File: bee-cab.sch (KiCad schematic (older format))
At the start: 26 parts, among them J1 Conn_01x02_Male, J10 Conn_01x01, J11 Conn_02x01, J12 Conn_02x01, J13 Conn_01x02, J14 Conn_01x02, J15 Conn_01x02, J16 Conn_01x02, J17 Conn_01x03, J18 Conn_01x02, J19 Conn_01x02, J2 Conn_01x02_Male, J3 Conn_01x02_Male, J4 Conn_01x02_Male, J5 Conn_01x03, J6 Conn_02x03_Odd_Even, J7 Conn_02x01, J8 Conn_01x02, J9 Conn_01x02

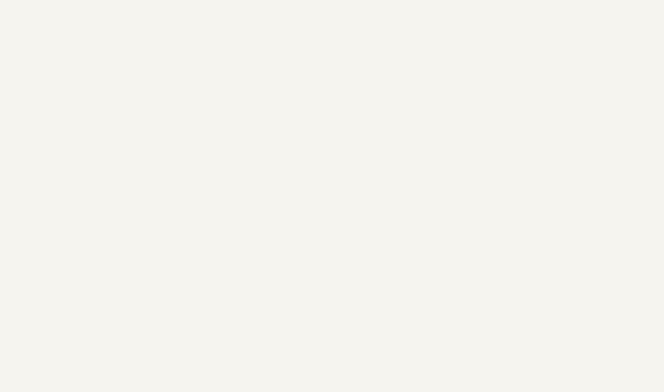
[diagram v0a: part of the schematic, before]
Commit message: Add sch symbols for labels, update PCB accordingly.
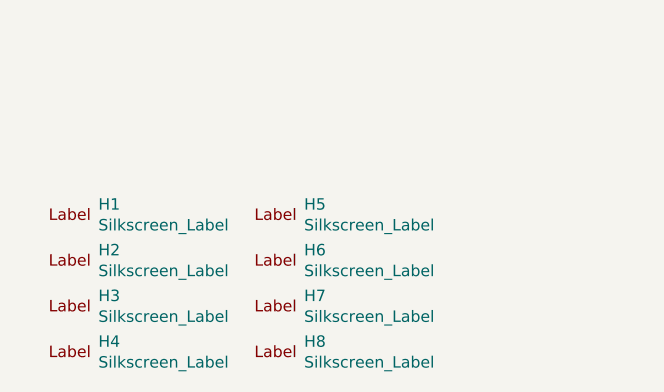
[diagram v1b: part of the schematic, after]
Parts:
- added H1, H2: Silkscreen_Label, Symbol-emt:Text_U_B+_Silkscreen, symbol Mechanical-emt:Silkscreen_Label
- added H3, H4: Silkscreen_Label, Symbol-emt:Text_U_B-_Silkscreen, symbol Mechanical-emt:Silkscreen_Label
- added H5, H6: Silkscreen_Label, Symbol-emt:Text_U_B2_Silkscreen, symbol Mechanical-emt:Silkscreen_Label
- added H7, H8: Silkscreen_Label, Symbol-emt:Symbol_GND_Silkscreen, symbol Mechanical-emt:Silkscreen_Label
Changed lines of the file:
@@
 Wire Wire Line
 	2600 2900 2600 3050
+$Comp
+L Mechanical-emt:Silkscreen_Label H4
+U 1 1 5CC7DACB
+P 800 7550
+F 0 "H4" H 925 7595 50  0000 L CNN
+F 1 "Silkscreen_Label" H 925 7504 50  0000 L CNN
+F 2 "Symbol-emt:Text_U_B-_Silkscreen" H 800 7550 50  0001 C CNN
+F 3 "~" H 800 7550 50  0001 C CNN
+	1    800  7550
+	1    0    0    -1
+$EndComp
+$Comp
+L Mechanical-emt:Silkscreen_Label H3
+U 1 1 5CC7E4B0
+P 800 7350
+F 0 "H3" H 925 7395 50  0000 L CNN
+F 1 "Silkscreen_Label" H 925 7304 50  0000 L CNN
+F 2 "Symbol-emt:Text_U_B-_Silkscreen" H 800 7350 50  0001 C CNN
+F 3 "~" H 800 7350 50  0001 C CNN
+	1    800  7350
+	1    0    0    -1
+$EndComp
+$Comp
+L Mechanical-emt:Silkscreen_Label H2
+U 1 1 5CC7E7BF
+P 800 7150
+F 0 "H2" H 925 7195 50  0000 L CNN
+F 1 "Silkscreen_Label" H 925 7104 50  0000 L CNN
+F 2 "Symbol-emt:Text_U_B+_Silkscreen" H 800 7150 50  0001 C CNN
+F 3 "~" H 800 7150 50  0001 C CNN
+	1    800  7150
+	1    0    0    -1
+$EndComp
+$Comp
+L Mechanical-emt:Silkscreen_Label H1
+U 1 1 5CC7EB64
+P 800 6950
+F 0 "H1" H 925 6995 50  0000 L CNN
+F 1 "Silkscreen_Label" H 925 6904 50  0000 L CNN
+F 2 "Symbol-emt:Text_U_B+_Silkscreen" H 800 6950 50  0001 C CNN
+F 3 "~" H 800 6950 50  0001 C CNN
+	1    800  6950
+	1    0    0    -1
+$EndComp
+$Comp
+L Mechanical-emt:Silkscreen_Label H5
+U 1 1 5CC7EED7
+P 1700 6950
+F 0 "H5" H 1825 6995 50  0000 L CNN
+F 1 "Silkscreen_Label" H 1825 6904 50  0000 L CNN
+F 2 "Symbol-emt:Text_U_B2_Silkscreen" H 1700 6950 50  0001 C CNN
+F 3 "~" H 1700 6950 50  0001 C CNN
+	1    1700 6950
+	1    0    0    -1
+$EndComp
+$Comp
+L Mechanical-emt:Silkscreen_Label H6
+U 1 1 5CC7F429
+P 1700 7150
+F 0 "H6" H 1825 7195 50  0000 L CNN
+F 1 "Silkscreen_Label" H 1825 7104 50  0000 L CNN
+F 2 "Symbol-emt:Text_U_B2_Silkscreen" H 1700 7150 50  0001 C CNN
+F 3 "~" H 1700 7150 50  0001 C CNN
+	1    1700 7150
+	1    0    0    -1
+$EndComp
+$Comp
+L Mechanical-emt:Silkscreen_Label H7
+U 1 1 5CC7F75B
+P 1700 7350
+F 0 "H7" H 1825 7395 50  0000 L CNN
+F 1 "Silkscreen_Label" H 1825 7304 50  0000 L CNN
+F 2 "Symbol-emt:Symbol_GND_Silkscreen" H 1700 7350 50  0001 C CNN
+F 3 "~" H 1700 7350 50  0001 C CNN
+	1    1700 7350
+	1    0    0    -1
+$EndComp
+$Comp
+L Mechanical-emt:Silkscreen_Label H8
+U 1 1 5CC7FA9C
+P 1700 7550
+F 0 "H8" H 1825 7595 50  0000 L CNN
+F 1 "Silkscreen_Label" H 1825 7504 50  0000 L CNN
+F 2 "Symbol-emt:Symbol_GND_Silkscreen" H 1700 7550 50  0001 C CNN
+F 3 "~" H 1700 7550 50  0001 C CNN
+	1    1700 7550
+	1    0    0    -1
+$EndComp
 $EndSCHEMATC

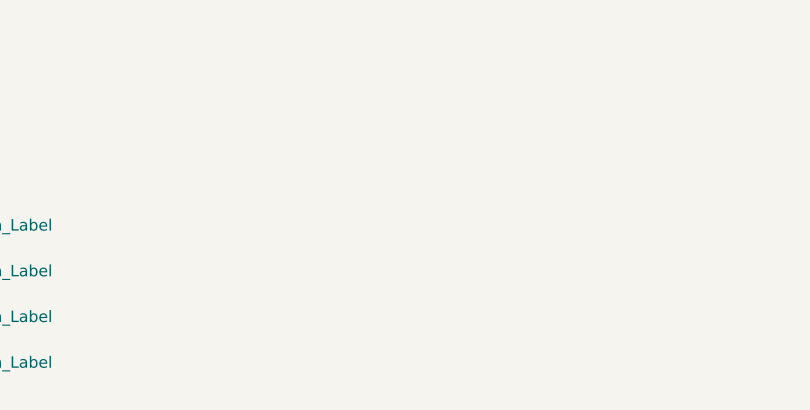
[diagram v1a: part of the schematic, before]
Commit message: Replace vias by mounting holes.
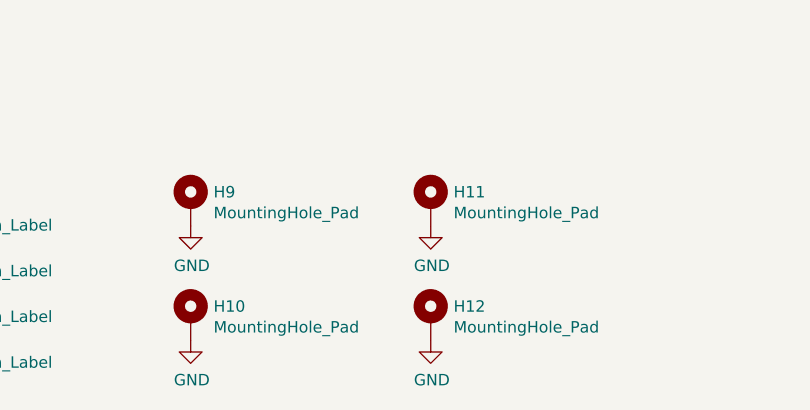
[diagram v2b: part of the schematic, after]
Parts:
- added H10, H11, H12, H9: MountingHole_Pad, MountingHole:MountingHole_3.2mm_M3_ISO7380_Pad, symbol Mechanical:MountingHole_Pad
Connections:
- net GND: now also H10.1, H11.1, H12.1, H9.1
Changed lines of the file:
@@
+	1    0    0    -1
+$EndComp
+$Comp
+L Mechanical:MountingHole_Pad H10
+U 1 1 5CC731BF
+P 3000 7400
+F 0 "H10" H 3100 7449 50  0000 L CNN
+F 1 "MountingHole_Pad" H 3100 7358 50  0000 L CNN
+F 2 "MountingHole:MountingHole_3.2mm_M3_ISO7380_Pad" H 3000 7400 50  0001 C CNN
+F 3 "~" H 3000 7400 50  0001 C CNN
+	1    3000 7400
+	1    0    0    -1
+$EndComp
+$Comp
+L power:GND #PWR0101
+U 1 1 5CC74B62
+P 3000 7500
+F 0 "#PWR0101" H 3000 7250 50  0001 C CNN
+F 1 "GND" H 3005 7327 50  0000 C CNN
+F 2 "" H 3000 7500 50  0001 C CNN
+F 3 "" H 3000 7500 50  0001 C CNN
+	1    3000 7500
+	1    0    0    -1
+$EndComp
+$Comp
+L Mechanical:MountingHole_Pad H9
+U 1 1 5CC7CF5D
+P 3000 6900
+F 0 "H9" H 3100 6949 50  0000 L CNN
+F 1 "MountingHole_Pad" H 3100 6858 50  0000 L CNN
+F 2 "MountingHole:MountingHole_3.2mm_M3_ISO7380_Pad" H 3000 6900 50  0001 C CNN
+F 3 "~" H 3000 6900 50  0001 C CNN
+	1    3000 6900
+	1    0    0    -1
+$EndComp
+$Comp
+L power:GND #PWR0102
+U 1 1 5CC7CF67
+P 3000 7000
+F 0 "#PWR0102" H 3000 6750 50  0001 C CNN
+F 1 "GND" H 3005 6827 50  0000 C CNN
+F 2 "" H 3000 7000 50  0001 C CNN
+F 3 "" H 3000 7000 50  0001 C CNN
+	1    3000 7000
+	1    0    0    -1
+$EndComp
+$Comp
+L Mechanical:MountingHole_Pad H12
+U 1 1 5CC82F8F
+P 4050 7400
+F 0 "H12" H 4150 7449 50  0000 L CNN
+F 1 "MountingHole_Pad" H 4150 7358 50  0000 L CNN
+F 2 "MountingHole:MountingHole_3.2mm_M3_ISO7380_Pad" H 4050 7400 50  0001 C CNN
+F 3 "~" H 4050 7400 50  0001 C CNN
+	1    4050 7400
+	1    0    0    -1
+$EndComp
+$Comp
+L power:GND #PWR0103
+U 1 1 5CC82F99
+P 4050 7500
+F 0 "#PWR0103" H 4050 7250 50  0001 C CNN
+F 1 "GND" H 4055 7327 50  0000 C CNN
+F 2 "" H 4050 7500 50  0001 C CNN
+F 3 "" H 4050 7500 50  0001 C CNN
+	1    4050 7500
+	1    0    0    -1
+$EndComp
+$Comp
+L Mechanical:MountingHole_Pad H11
+U 1 1 5CC82FA3
+P 4050 6900
+F 0 "H11" H 4150 6949 50  0000 L CNN
+F 1 "MountingHole_Pad" H 4150 6858 50  0000 L CNN
+F 2 "MountingHole:MountingHole_3.2mm_M3_ISO7380_Pad" H 4050 6900 50  0001 C CNN
+F 3 "~" H 4050 6900 50  0001 C CNN
+	1    4050 6900
+	1    0    0    -1
+$EndComp
+$Comp
+L power:GND #PWR0104
+U 1 1 5CC82FAD
+P 4050 7000
+F 0 "#PWR0104" H 4050 6750 50  0001 C CNN
+F 1 "GND" H 4055 6827 50  0000 C CNN
+F 2 "" H 4050 7000 50  0001 C CNN
+F 3 "" H 4050 7000 50  0001 C CNN
+	1    4050 7000
 	1    0    0    -1
 $EndComp

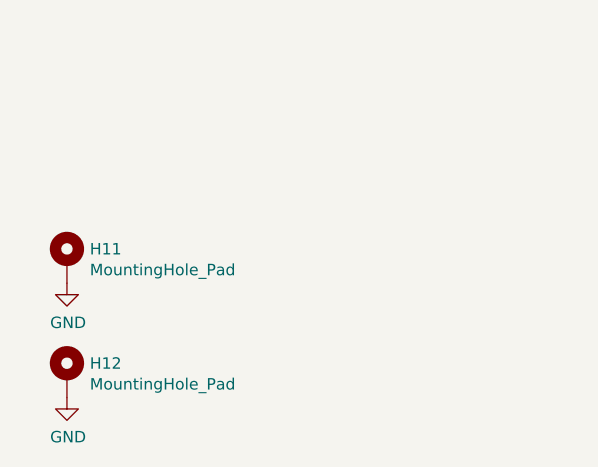
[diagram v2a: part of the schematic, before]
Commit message: Add text and logos.
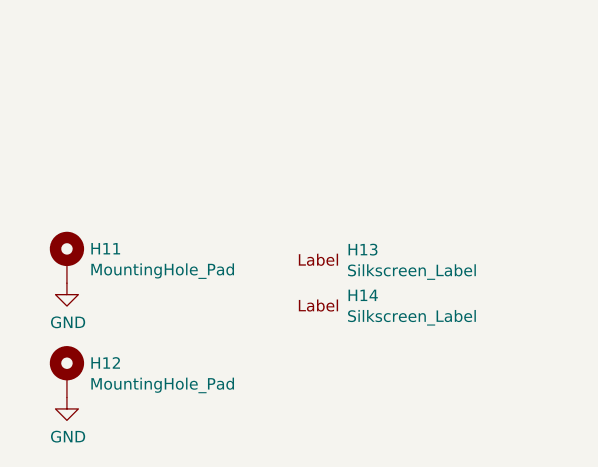
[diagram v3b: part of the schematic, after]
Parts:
- added H13: Silkscreen_Label, Symbol-emt:EMT-Logo_5.1x2.5mm_Silkscreen, symbol Mechanical-emt:Silkscreen_Label
- added H14: Silkscreen_Label, Symbol-emt:BEE-Logo_Silkscreen_small, symbol Mechanical-emt:Silkscreen_Label
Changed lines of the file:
@@
 EESchema Schematic File Version 4
 LIBS:bee-cab-cache
-EELAYER 29 0
+EELAYER 26 0
 EELAYER END
 $Descr A4 11693 8268
@@
 	1    0    0    -1
 $EndComp
+$Comp
+L Mechanical-emt:Silkscreen_Label H13
+U 1 1 5CCCFACF
+P 5150 6900
+F 0 "H13" H 5275 6945 50  0000 L CNN
+F 1 "Silkscreen_Label" H 5275 6854 50  0000 L CNN
+F 2 "Symbol-emt:EMT-Logo_5.1x2.5mm_Silkscreen" H 5150 6900 50  0001 C CNN
+F 3 "~" H 5150 6900 50  0001 C CNN
+	1    5150 6900
+	1    0    0    -1
+$EndComp
+$Comp
+L Mechanical-emt:Silkscreen_Label H14
+U 1 1 5CCCFB83
+P 5150 7100
+F 0 "H14" H 5275 7145 50  0000 L CNN
+F 1 "Silkscreen_Label" H 5275 7054 50  0000 L CNN
+F 2 "Symbol-emt:BEE-Logo_Silkscreen_small" H 5150 7100 50  0001 C CNN
+F 3 "~" H 5150 7100 50  0001 C CNN
+	1    5150 7100
+	1    0    0    -1
+$EndComp

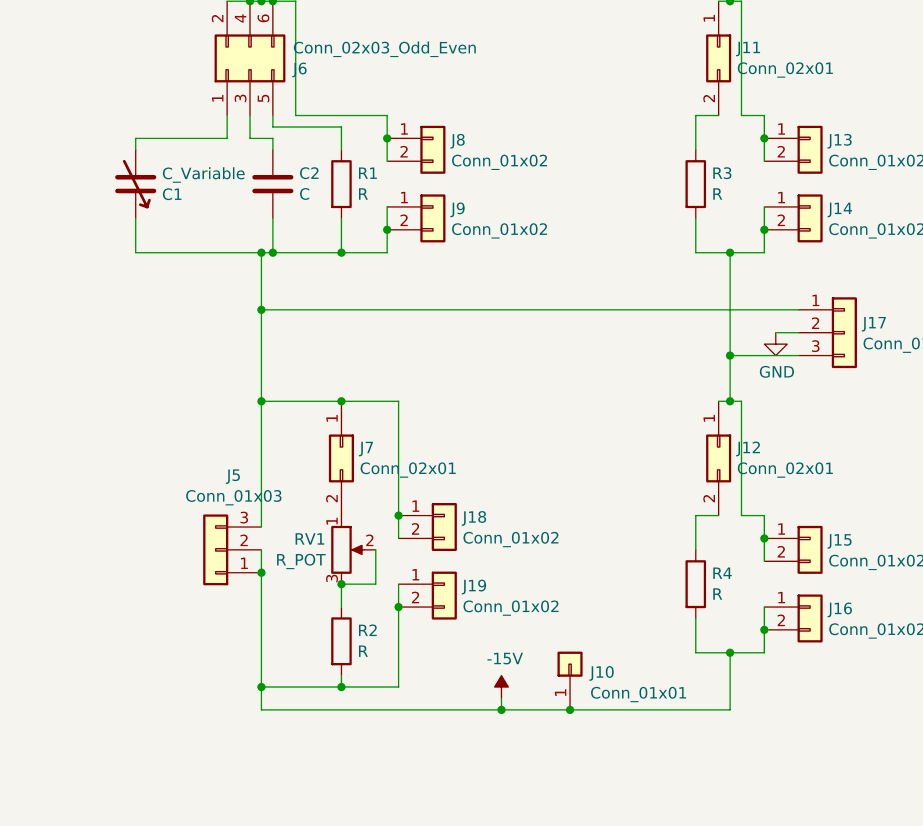
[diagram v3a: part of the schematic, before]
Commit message: Add part numbers.
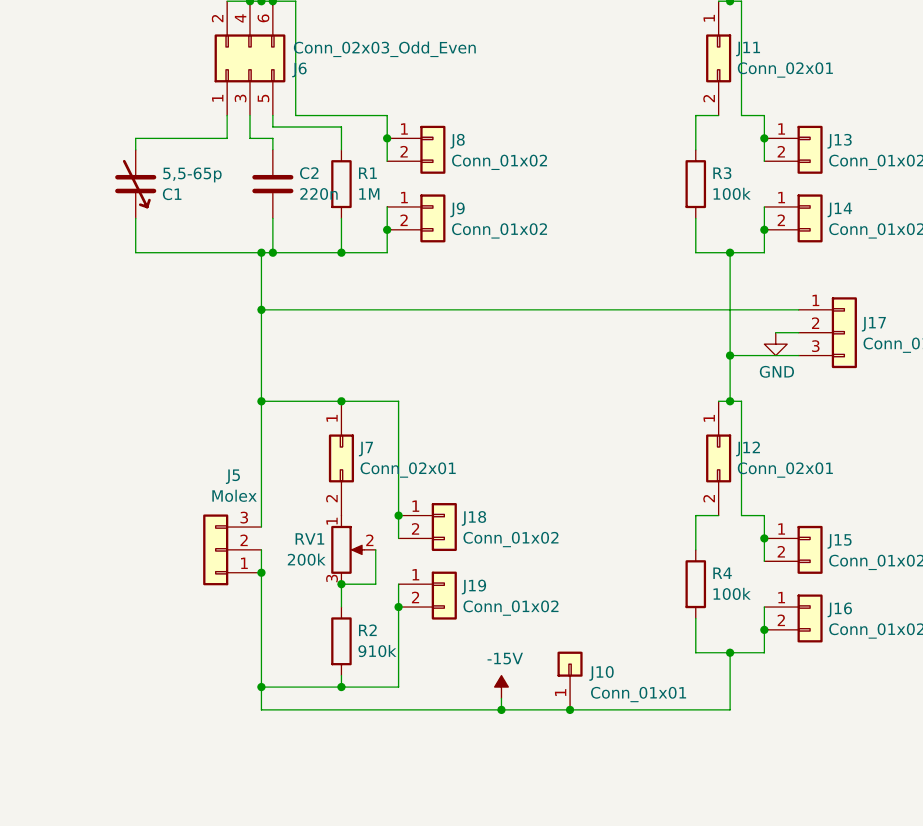
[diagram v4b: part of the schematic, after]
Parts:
- C1: value C_Variable -> 5,5-65p; Reichelt Part No (none) -> TRIMMER 31659
- C2: value C -> 220n; Reichelt Part No (none) -> X7R 0805 CF 220N
- J1, J11, J12, J2, J3, J4, J7: Reichelt Part No (none) -> RND 205-00623
- J10: Reichelt Part No (none) -> RND 205-00622
- J13, J14, J15, J16, J18, J19, J8, J9: Reichelt Part No (none) -> MPE 006-1-002
- J17: Reichelt Part No (none) -> RND 205-00624
- J5: value Conn_01x03 -> Molex; Manufacturer (none) -> Molex; Manufacturer Part No (none) -> 52807-0310; Mouser Part No (none) -> 538-52807-0310
- J6: Reichelt Part No (none) -> RND 205-00634
- R1: value R -> 1M; Reichelt Part No (none) -> RND 0805 1 1,0M
- R2: value R -> 910k; Reichelt Part No (none) -> RND 0805 1 910K
- R3, R4: value R -> 100k; Reichelt Part No (none) -> RND 0805 1 100K
- RV1: value R_POT -> 200k; Reichelt Part No (none) -> 64W-200K
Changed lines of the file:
@@
 F 2 "Connector_PinHeader_2.54mm:PinHeader_1x02_P2.54mm_Vertical" H 850 1300 50  0001 C CNN
 F 3 "~" H 850 1300 50  0001 C CNN
+F 4 "RND 205-00623" H 850 1300 50  0001 C CNN "Reichelt Part No"
 	1    850  1300
 	1    0    0    -1
@@
 F 2 "Connector_PinHeader_2.54mm:PinHeader_1x02_P2.54mm_Vertical" H 850 950 50  0001 C CNN
 F 3 "~" H 850 950 50  0001 C CNN
+F 4 "RND 205-00623" H 850 950 50  0001 C CNN "Reichelt Part No"
 	1    850  950
 	1    0    0    -1
@@
 F 2 "Connector_PinHeader_2.54mm:PinHeader_1x02_P2.54mm_Vertical" H 850 2150 50  0001 C CNN
 F 3 "~" H 850 2150 50  0001 C CNN
+F 4 "RND 205-00623" H 850 2150 50  0001 C CNN "Reichelt Part No"
 	1    850  2150
 	1    0    0    -1
@@
 F 2 "Connector_PinHeader_2.54mm:PinHeader_1x02_P2.54mm_Vertical" H 850 1800 50  0001 C CNN
 F 3 "~" H 850 1800 50  0001 C CNN
+F 4 "RND 205-00623" H 850 1800 50  0001 C CNN "Reichelt Part No"
 	1    850  1800
 	1    0    0    -1
@@
 P 2600 2750
 F 0 "C1" H 2715 2796 50  0000 L CNN
-F 1 "C_Variable" H 2715 2705 50  0000 L CNN
+F 1 "5,5-65p" H 2715 2705 50  0000 L CNN
 F 2 "Capacitor_THT-emt:C_Trimmer_Vishay_D10mm_Vertical_HolePattern5mmx10mm" H 2600 2750 50  0001 C CNN
 F 3 "~" H 2600 2750 50  0001 C CNN
+F 4 "TRIMMER 31659" H 2600 2750 50  0001 C CNN "Reichelt Part No"
 	1    2600 2750
 	1    0    0    1
@@
 P 2950 4350
 F 0 "J5" H 2870 4025 50  0000 C CNN
-F 1 "Conn_01x03" H 2870 4116 50  0000 C CNN
+F 1 "Molex" H 2870 4116 50  0000 C CNN
 F 2 "Connector_Molex-emt:Molex_Easy-On_528070310_1x03_P1.0mm_Horizontal" H 2950 4350 50  0001 C CNN
 F 3 "~" H 2950 4350 50  0001 C CNN
+F 4 "538-52807-0310" H 2950 4350 50  0001 C CNN "Mouser Part No"
+F 5 "Molex" H 2950 4350 50  0001 C CNN "Manufacturer"
+F 6 "52807-0310" H 2950 4350 50  0001 C CNN "Manufacturer Part No"
 	1    2950 4350
 	-1   0    0    1
@@
 P 3200 2750
 F 0 "C2" H 3315 2796 50  0000 L CNN
-F 1 "C" H 3315 2705 50  0000 L CNN
+F 1 "220n" H 3315 2705 50  0000 L CNN
 F 2 "Capacitor_SMD:C_0805_2012Metric_Pad1.15x1.40mm_HandSolder" H 3238 2600 50  0001 C CNN
 F 3 "~" H 3200 2750 50  0001 C CNN
+F 4 "X7R 0805 CF 220N" H 3200 2750 50  0001 C CNN "Reichelt Part No"
 	1    3200 2750
 	1    0    0    -1
@@
 F 2 "Connector_PinSocket_2.54mm:PinSocket_2x01_P2.54mm_Vertical" H 3900 2550 50  0001 C CNN
 F 3 "~" H 3900 2550 50  0001 C CNN
+F 4 "MPE 006-1-002" H 3900 2550 50  0001 C CNN "Reichelt Part No"
 	1    3900 2550
 	1    0    0    -1
@@
 F 2 "Connector_PinSocket_2.54mm:PinSocket_2x01_P2.54mm_Vertical" H 3900 2850 50  0001 C CNN
 F 3 "~" H 3900 2850 50  0001 C CNN
+F 4 "MPE 006-1-002" H 3900 2850 50  0001 C CNN "Reichelt Part No"
 	1    3900 2850
 	1    0    0    -1
@@
 P 3500 2750
 F 0 "R1" H 3570 2796 50  0000 L CNN
-F 1 "R" H 3570 2705 50  0000 L CNN
+F 1 "1M" H 3570 2705 50  0000 L CNN
 F 2 "Resistor_SMD:R_0805_2012Metric_Pad1.15x1.40mm_HandSolder" V 3430 2750 50  0001 C CNN
 F 3 "~" H 3500 2750 50  0001 C CNN
+F 4 "RND 0805 1 1,0M" H 3500 2750 50  0001 C CNN "Reichelt Part No"
 	1    3500 2750
 	1    0    0    -1
@@
 P 5050 2750
 F 0 "R3" H 5120 2796 50  0000 L CNN
-F 1 "R" H 5120 2705 50  0000 L CNN
+F 1 "100k" H 5120 2705 50  0000 L CNN
 F 2 "Resistor_SMD:R_0805_2012Metric_Pad1.15x1.40mm_HandSolder" V 4980 2750 50  0001 C CNN
 F 3 "~" H 5050 2750 50  0001 C CNN
+F 4 "RND 0805 1 100K" H 5050 2750 50  0001 C CNN "Reichelt Part No"
 	1    5050 2750
 	1    0    0    -1
@@
 P 5050 4500
 F 0 "R4" H 5120 4546 50  0000 L CNN
-F 1 "R" H 5120 4455 50  0000 L CNN
+F 1 "100k" H 5120 4455 50  0000 L CNN
 F 2 "Resistor_SMD:R_0805_2012Metric_Pad1.15x1.40mm_HandSolder" V 4980 4500 50  0001 C CNN
 F 3 "~" H 5050 4500 50  0001 C CNN
+F 4 "RND 0805 1 100K" H 5050 4500 50  0001 C CNN "Reichelt Part No"
 	1    5050 4500
 	1    0    0    -1
@@
 P 3500 4750
 F 0 "R2" H 3570 4796 50  0000 L CNN
-F 1 "R" H 3570 4705 50  0000 L CNN
+F 1 "910k" H 3570 4705 50  0000 L CNN
 F 2 "Resistor_SMD:R_0805_2012Metric_Pad1.15x1.40mm_HandSolder" V 3430 4750 50  0001 C CNN
 F 3 "~" H 3500 4750 50  0001 C CNN
+F 4 "RND 0805 1 910K" H 3500 4750 50  0001 C CNN "Reichelt Part No"
 	1    3500 4750
 	1    0    0    -1
@@
 F 2 "Connector_PinHeader_2.54mm:PinHeader_1x01_P2.54mm_Vertical" H 4500 4850 50  0001 C CNN
 F 3 "~" H 4500 4850 50  0001 C CNN
+F 4 "RND 205-00622" H 4500 4850 50  0001 C CNN "Reichelt Part No"
 	1    4500 4850
 	0    -1   -1   0
@@
 F 2 "Connector_PinSocket_2.54mm:PinSocket_2x01_P2.54mm_Vertical" H 5550 4300 50  0001 C CNN
 F 3 "~" H 5550 4300 50  0001 C CNN
+F 4 "MPE 006-1-002" H 5550 4300 50  0001 C CNN "Reichelt Part No"
 	1    5550 4300
 	1    0    0    -1
@@
 F 2 "Connector_PinSocket_2.54mm:PinSocket_2x01_P2.54mm_Vertical" H 5550 4600 50  0001 C CNN
 F 3 "~" H 5550 4600 50  0001 C CNN
+F 4 "MPE 006-1-002" H 5550 4600 50  0001 C CNN "Reichelt Part No"
 	1    5550 4600
 	1    0    0    -1
@@
 F 2 "Connector_PinSocket_2.54mm:PinSocket_2x01_P2.54mm_Vertical" H 5550 2550 50  0001 C CNN
 F 3 "~" H 5550 2550 50  0001 C CNN
+F 4 "MPE 006-1-002" H 5550 2550 50  0001 C CNN "Reichelt Part No"
 	1    5550 2550
 	1    0    0    -1
@@
 F 2 "Connector_PinSocket_2.54mm:PinSocket_2x01_P2.54mm_Vertical" H 5550 2850 50  0001 C CNN
 F 3 "~" H 5550 2850 50  0001 C CNN
+F 4 "MPE 006-1-002" H 5550 2850 50  0001 C CNN "Reichelt Part No"
 	1    5550 2850
 	1    0    0    -1
@@
 P 3500 4350
 F 0 "RV1" H 3431 4396 50  0000 R CNN
-F 1 "R_POT" H 3431 4305 50  0000 R CNN
+F 1 "200k" H 3431 4305 50  0000 R CNN
 F 2 "Potentiometer_THT:Potentiometer_Bourns_3296W_Vertical" H 3500 4350 50  0001 C CNN
 F 3 "~" H 3500 4350 50  0001 C CNN
+F 4 "64W-200K" H 3500 4350 50  0001 C CNN "Reichelt Part No"
 	1    3500 4350
 	1    0    0    -1
@@
 F 2 "Connector_PinHeader_2.54mm:PinHeader_2x01_P2.54mm_Vertical" H 3500 3900 50  0001 C CNN
 F 3 "~" H 3500 3900 50  0001 C CNN
+F 4 "RND 205-00623" H 3500 3900 50  0001 C CNN "Reichelt Part No"
 	1    3500 3900
 	0    1    1    0
@@
 F 2 "Connector_PinHeader_2.54mm:PinHeader_1x03_P2.54mm_Vertical" H 5700 3400 50  0001 C CNN
 F 3 "~" H 5700 3400 50  0001 C CNN
+F 4 "RND 205-00624" H 5700 3400 50  0001 C CNN "Reichelt Part No"
 	1    5700 3400
 	1    0    0    -1
@@
 F 2 "Connector_PinHeader_2.54mm:PinHeader_2x03_P2.54mm_Vertical" H 3100 2250 50  0001 C CNN
 F 3 "~" H 3100 2250 50  0001 C CNN
+F 4 "RND 205-00634" H 3100 2250 50  0001 C CNN "Reichelt Part No"
 	1    3100 2250
 	0    -1   -1   0
@@
 F 2 "Connector_PinHeader_2.54mm:PinHeader_2x01_P2.54mm_Vertical" H 5150 2150 50  0001 C CNN
 F 3 "~" H 5150 2150 50  0001 C CNN
+F 4 "RND 205-00623" H 5150 2150 50  0001 C CNN "Reichelt Part No"
 	1    5150 2150
 	0    1    1    0
@@
 F 2 "Connector_PinHeader_2.54mm:PinHeader_2x01_P2.54mm_Vertical" H 5150 3900 50  0001 C CNN
 F 3 "~" H 5150 3900 50  0001 C CNN
+F 4 "RND 205-00623" H 5150 3900 50  0001 C CNN "Reichelt Part No"
 	1    5150 3900
 	0    1    1    0
@@
 F 2 "Connector_PinSocket_2.54mm:PinSocket_2x01_P2.54mm_Vertical" H 3950 4200 50  0001 C CNN
 F 3 "~" H 3950 4200 50  0001 C CNN
+F 4 "MPE 006-1-002" H 3950 4200 50  0001 C CNN "Reichelt Part No"
 	1    3950 4200
 	1    0    0    -1
@@
 F 2 "Connector_PinSocket_2.54mm:PinSocket_2x01_P2.54mm_Vertical" H 3950 4500 50  0001 C CNN
 F 3 "~" H 3950 4500 50  0001 C CNN
+F 4 "MPE 006-1-002" H 3950 4500 50  0001 C CNN "Reichelt Part No"
 	1    3950 4500
 	1    0    0    -1
